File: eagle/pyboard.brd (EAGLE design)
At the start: 34 x 40 mm, 58 parts, among them IC1 STM32F405RGT, Q1 8MHz, Q2 32.768kHz, U1 MCP1802

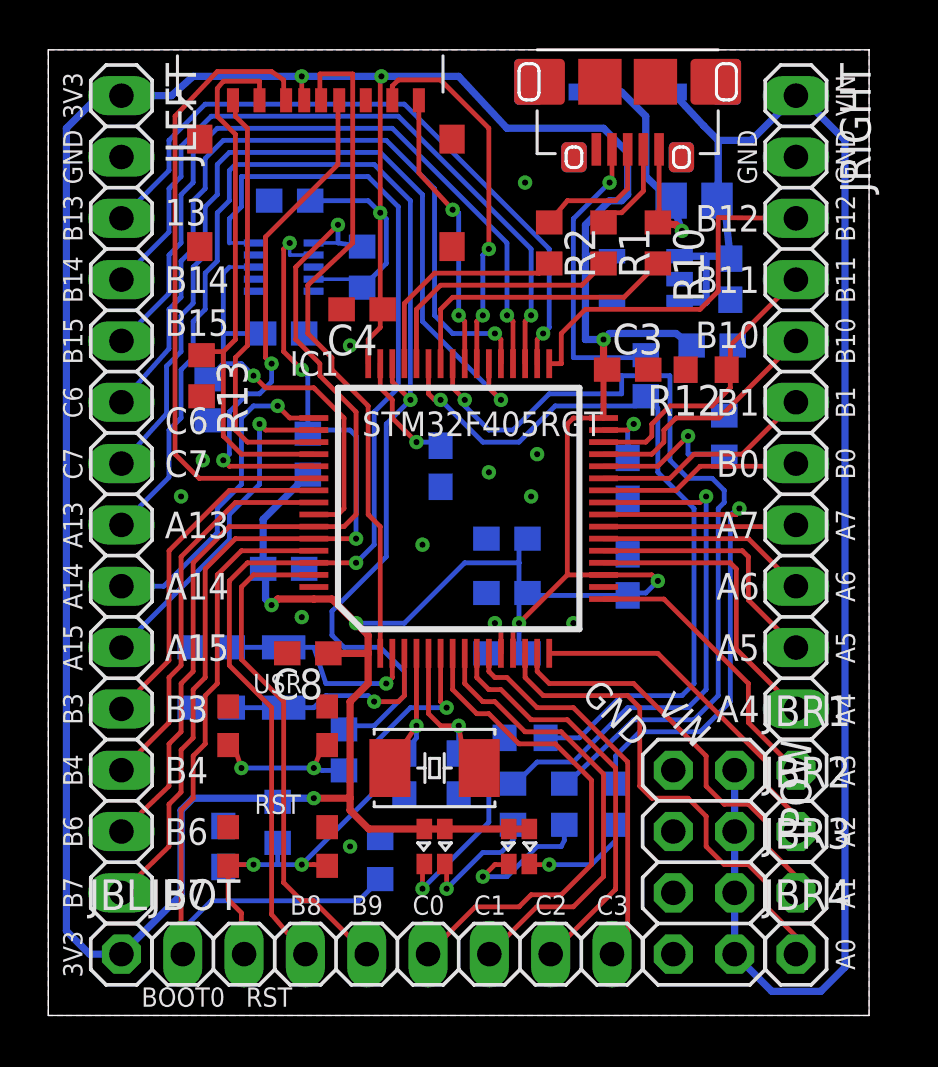
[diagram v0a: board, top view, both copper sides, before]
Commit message: updated pyboard to more closely resemble the newer v10 boards for which eagle files aren't available yet
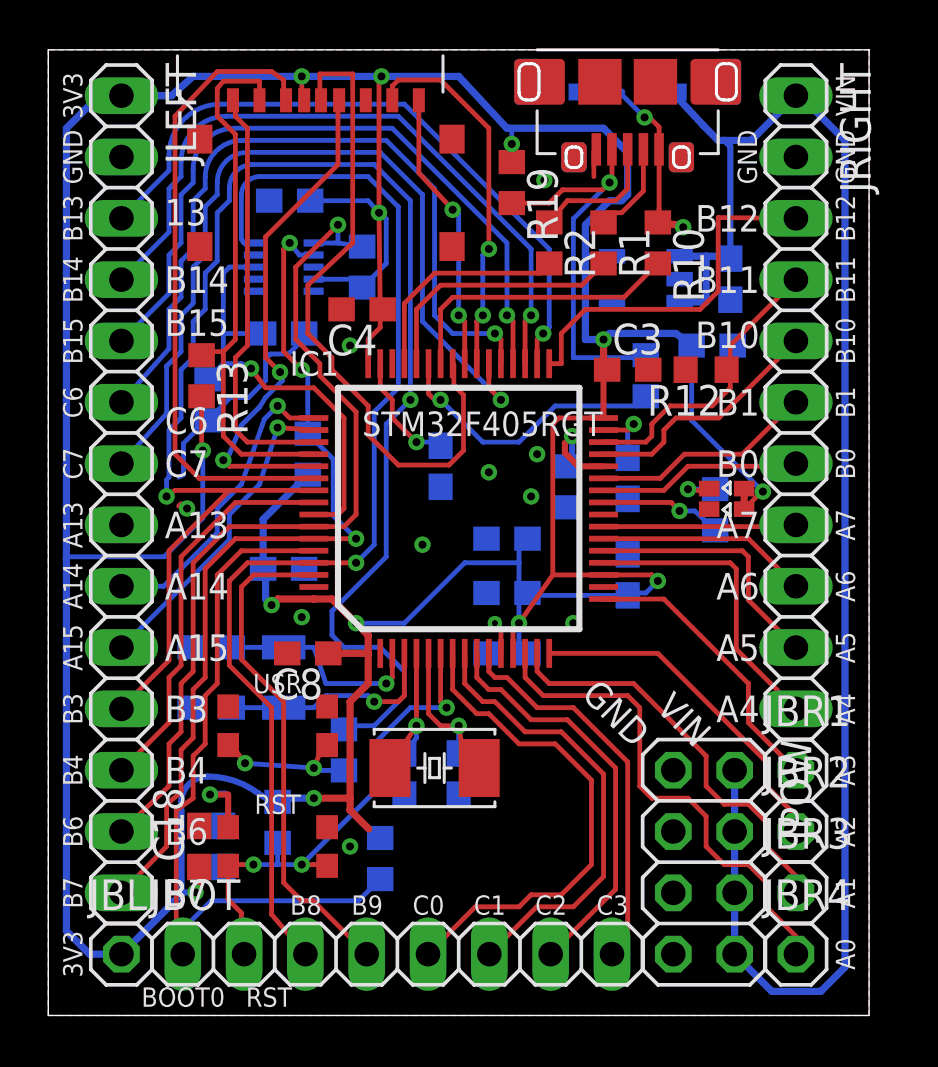
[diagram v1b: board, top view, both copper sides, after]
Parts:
- removed R11: 1k, rcl:R0603
- removed R4, R5, R7: 560, rcl:R0603
- removed U$6: LTST-C195KGJRKT, pyboard:LTST-BILED-15X16
- added C18: 4u7, rcl:C0603
- added R19: 100k, rcl:R0603
- C11, C12: value 12p -> 2p2
- C16, C17: value 1u -> 2u2
- R10: value 1k -> 560R
- R13: value 10M -> 100k
- R16: value 0 -> 560R
- R18: value 0 -> 100k; device rcl:R0805 -> rcl:R0603
- R3: value 10k -> 4k7
- moved U$1 16.8 mm to (28.1, 21.4), turned to 270 degrees
- moved R6 13.7 mm to (27.6, 20.9), turned to 90 degrees
- moved R18 13.0 mm to (21.4, 21.9), turned to 270 degrees
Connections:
- removed net IO_PB2: IC1.28, R11.1
- removed net IO_PB3: IC1.55, JLEFT.11
- removed net IO_PB4: IC1.56, JLEFT.12
- removed net LEDG1: IC1.24, R4.1
- removed net N$11: R4.2, U$1.P$3
- removed net N$12: R5.2, U$6.P$4
- removed net N$14: R7.2, U$6.P$3
- new net N$8: IC1.28, R18.1
- net +3V3: now also C18.1, R13.2, R19.1; no longer U$6.P$1, U$6.P$2
- net GND: now also C18.2, R18.2; no longer R11.2, R13.2
- net LEDG2: now also IC1.56, JLEFT.12; no longer IC1.25, R7.1
- net LEDR1: now also IC1.25; no longer IC1.41
- net LEDR2: no longer R5.1
- net N$7: now also R19.2
- net SDIO_SW: now also IC1.41; no longer IC1.2
- net USR_SW: now also IC1.55, JLEFT.11; no longer IC1.46, JLEFT.8
- net VIN: no longer R18.1
- net VUSB: no longer R18.2
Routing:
- net LEDR1: track 35.1 -> 5.09 mm
- net LEDG1: track 20.8 -> 0.00 mm, vias 1 -> 0
- net LEDR2: track 31.7 -> 11.9 mm
- net +3V3: track 179.5 -> 198.2 mm, vias 9 -> 13
- net IO_PB4: track 16.3 -> 0.00 mm
- net IO_PB3: track 14.4 -> 0.00 mm
- net GND: track 1.35 -> 14.4 mm
- net USR_SW: track 53.6 -> 66.5 mm, vias 1 -> 2
- net N$12: track 8.67 -> 0.00 mm, vias 1 -> 0
- net IO_PB2: track 6.28 -> 0.00 mm, vias 1 -> 0
- net LEDG2: track 22.1 -> 16.3 mm, vias 1 -> 0
- net N$14: track 5.26 -> 0.00 mm, vias 1 -> 0
- net N$11: track 4.64 -> 0.00 mm, vias 1 -> 0
- net N$7: track 12.3 -> 16.7 mm
- net N$8: track 0.00 -> 4.01 mm, vias 0 -> 1
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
